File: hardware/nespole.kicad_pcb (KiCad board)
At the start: 2 copper layers, 26.4 x 50.5 mm, 19 parts, among them IC1 ATTINY25-20SSU, J1 Screw_Terminal_1x02, J2 Screw_Terminal_1x02, J3 ICSP, P1 USB_OTG, Q1 IRF510, U1 MAX31855KASA, U2 AP1117, U3 CH340G, Y1 12M

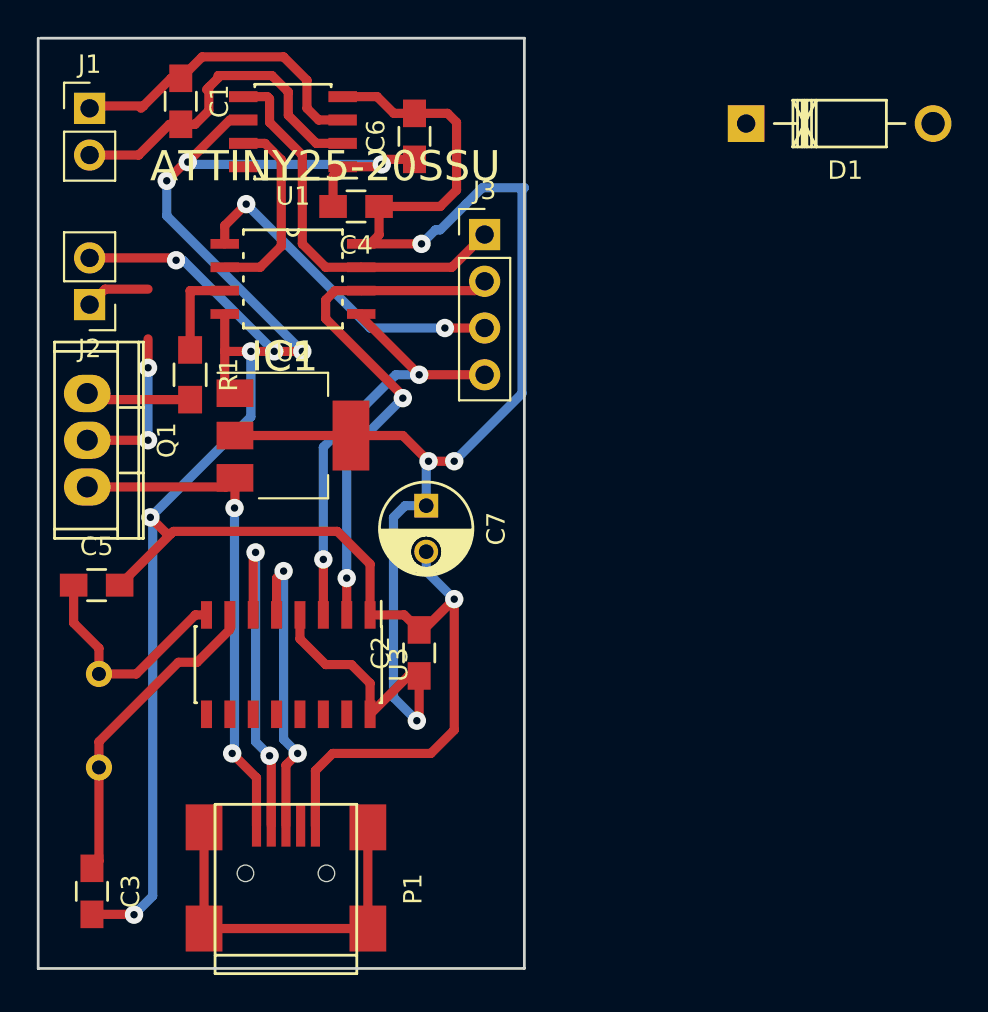
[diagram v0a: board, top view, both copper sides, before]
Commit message: Updating board to use mosfet for switching relay on/off.
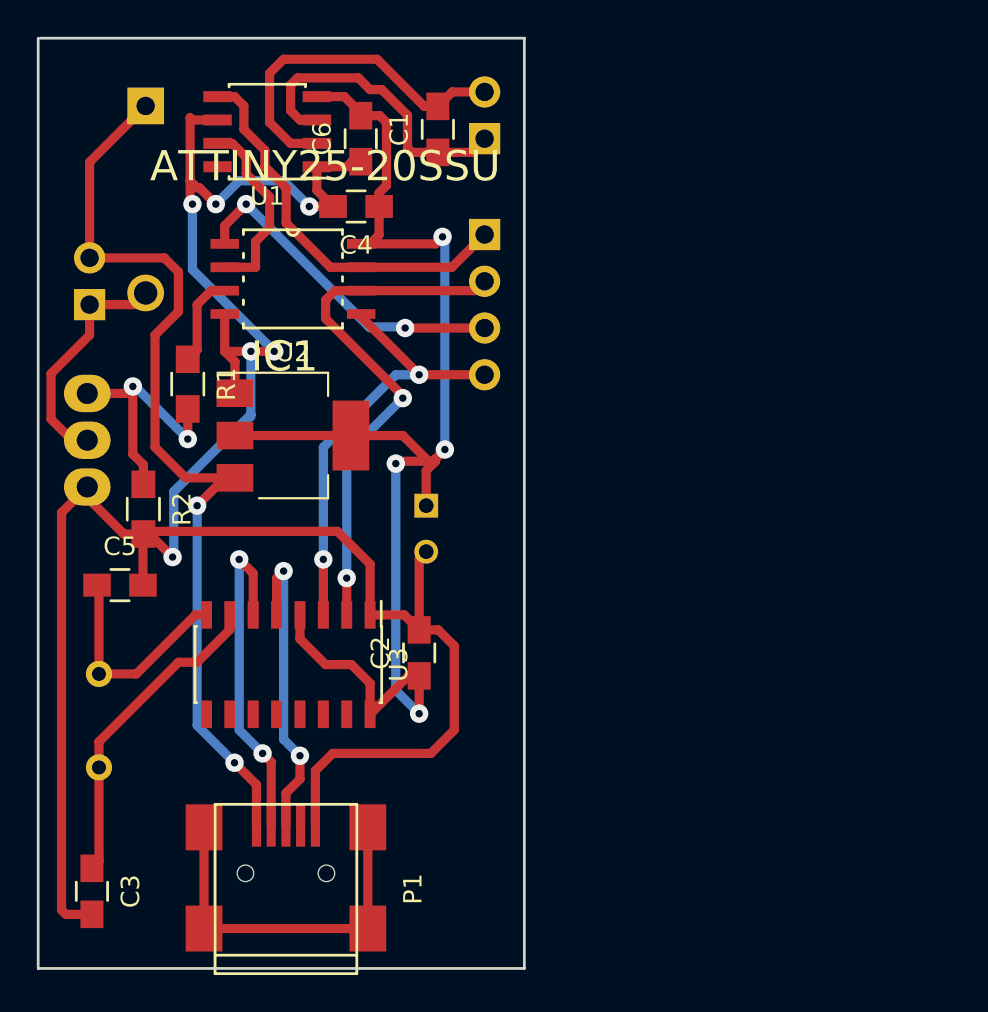
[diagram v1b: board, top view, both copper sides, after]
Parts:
- added R2: 10k, Resistors_SMD:R_0805_HandSoldering, F.Cu at (144.5, 105.5)
- C7, D1, J1, J2, J3, Q1: moved to B.Cu
- moved D1 32.6 mm to (144.7, 83.6), turned to 270 degrees
- moved J1 21.5 mm to (163.1, 85.3)
- moved C1 14.1 mm to (160.5, 84.8), turned to 90 degrees
- moved C6 2.92 mm to (156.3, 85.3)
- moved U1 1.40 mm to (151.3, 85.0)
- moved C5 1.27 mm to (143.3, 109.6)
- moved R1 0.52 mm to (146.9, 98.7)
- turned J2 to 0 degrees
- turned J3 to 180 degrees
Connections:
- J2 pad 2: Net-(J2-Pad2) -> +5V
- Q1 pad 2: GND -> /to_relay
- Q1 pad 3: Net-(J2-Pad2) -> GND
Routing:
- net +5V: track 20.9 -> 51.1 mm
- net Net-(J2-Pad2): track 19.7 -> 0.00 mm, vias 1 -> 0
- net +3V3: track 87.1 -> 72.4 mm
- net /to_relay: track 3.52 -> 13.5 mm
- net Net-(Q1-Pad1): track 5.73 -> 14.5 mm, vias 0 -> 2
- net GND: track 135.4 -> 127.4 mm, vias 11 -> 6
- net Net-(C1-Pad1): track 17.4 -> 16.8 mm
- net Net-(C5-Pad1): track 12.6 -> 12.0 mm
